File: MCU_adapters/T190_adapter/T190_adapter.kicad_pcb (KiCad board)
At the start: 2 copper layers, 35 x 60.6 mm, 5 parts, among them J1 Conn_01x22, J2 Conn_01x22, J3 Conn_01x12_Socket, J4 Conn_01x12_Socket

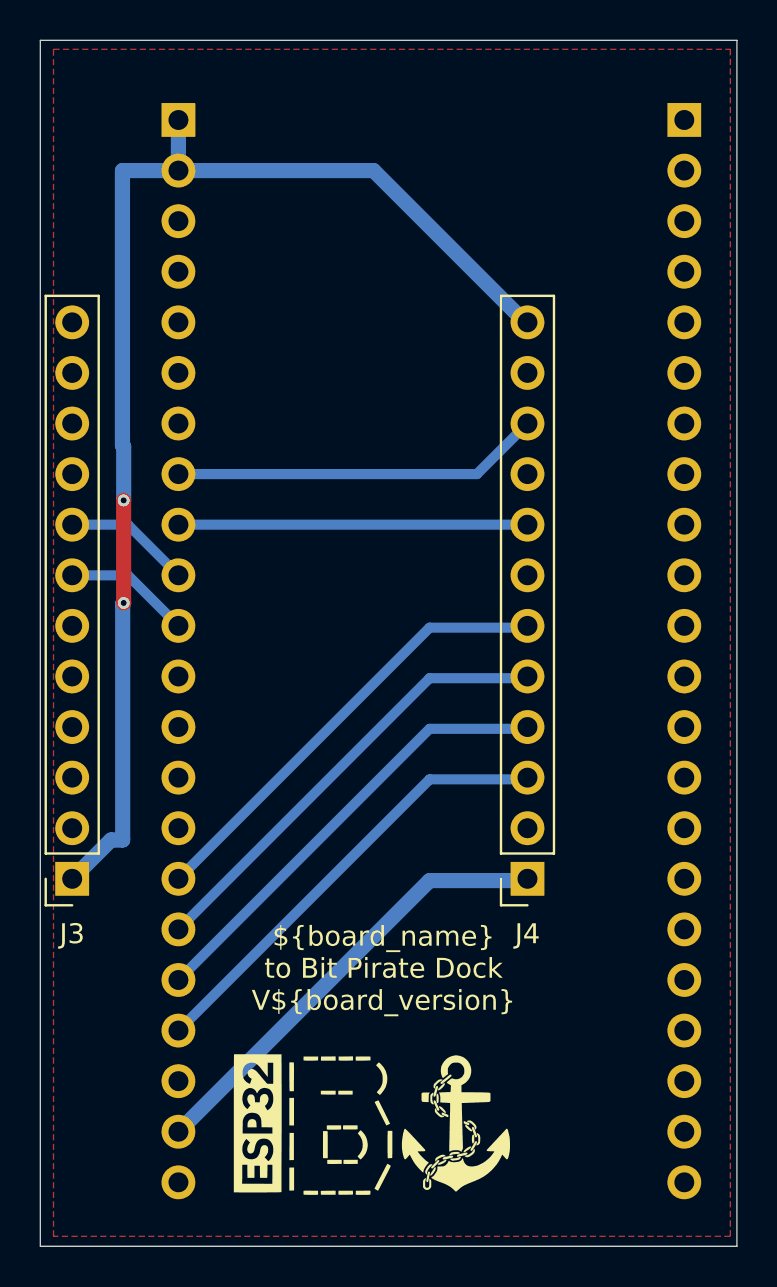
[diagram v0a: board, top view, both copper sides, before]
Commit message: Updated adapters with USB logo
Added an USB logo to ensure the card is inserted the right way up.
Added an USB logo in the logo library
Updated the gerber files
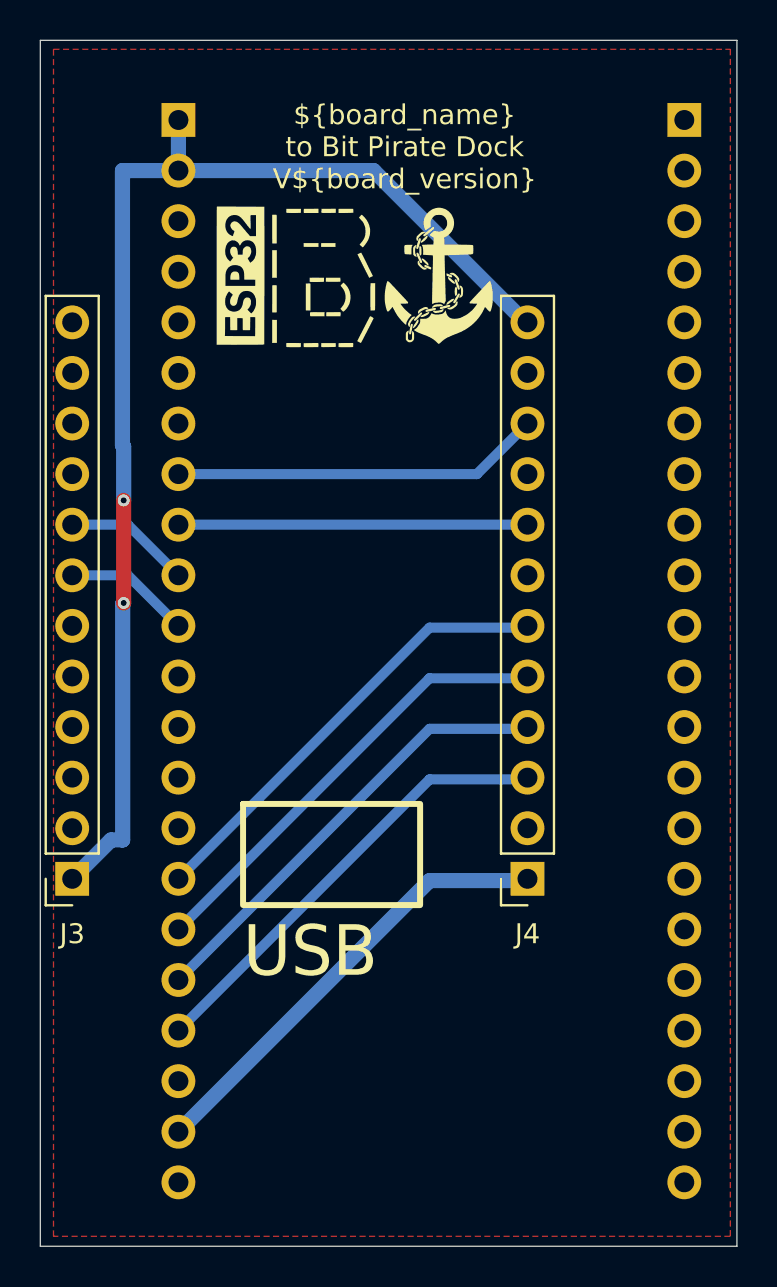
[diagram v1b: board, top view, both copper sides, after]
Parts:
- added G2: ~, logo:LOGO_USB, F.Cu at (84.5, 59.7)
- moved G1 42.6 mm to (84.9, 35.0)
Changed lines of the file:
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@@
 	(footprint "logo:logoBP"
 		(layer "F.Cu")
-		(at 85.773212 77.5912)
+		(at 84.91 35.03)
 		(property "Reference" "G1"
 			(at 0 -0.5 0)
@@
 		(embedded_fonts no)
 	)
+	(footprint "logo:LOGO_USB"
+		(layer "F.Cu")
+		(at 84.525 59.74)
+		(property "Reference" "G2"
+			(at 0 -0.5 0)
+			(unlocked yes)
+			(layer "F.SilkS")
+			(hide yes)
+			(effects
+				(font
+					(size 1 1)
+					(thickness 0.15)
+				)
+			)
+		)
+		(property "Value" "~"
+			(at 0 1 0)
+			(unlocked yes)
+			(layer "F.Fab")
+			(effects
+				(font
+					(size 1 1)
+					(thickness 0.15)
+				)
+			)
+		)
+		(property "Datasheet" ""
+			(at 0 0 0)
+			(unlocked yes)
+			(layer "F.Fab")
+			(hide yes)
+			(effects
+				(font
+					(size 1 1)
+					(thickness 0.15)
+				)
+			)
+		)
+		(property "Description" ""
+			(at 0 0 0)
+			(unlocked yes)
+			(layer "F.Fab")
+			(hide yes)
+			(effects
+				(font
+					(size 1 1)
+					(thickness 0.15)
+				)
+			)
+		)
+		(sheetname "/")
+		(sheetfile "T190_adapter.kicad_sch")
+		(units
+			(unit
+				(name "A")
+				(pins)
+			)
+		)
+		(attr smd exclude_from_bom)
+		(duplicate_pad_numbers_are_jumpers no)
+		(fp_rect
+			(start -5.08 0)
+			(end 3.81 5.08)
+			(stroke
+				(width 0.3)
+				(type solid)
+			)
+			(fill no)
+			(layer "F.SilkS")
+		)
+		(fp_text user "USB"
+			(at -5.08 8.89 0)
+			(unlocked yes)
+			(layer "F.SilkS")
+			(effects
+				(font
+					(size 2.54 2.4)
+					(thickness 0.25)
+				)
+				(justify left bottom)
+			)
+		)
+		(fp_text user "${REFERENCE}"
+			(at 0 2.5 0)
+			(unlocked yes)
+			(layer "F.Fab")
+			(effects
+				(font
+					(size 1 1)
+					(thickness 0.15)
+				)
+			)
+		)
+		(embedded_fonts no)
+	)
 	(footprint "Connector_PinHeader_2.54mm:PinHeader_1x22_P2.54mm_Vertical"
 		(locked yes)
@@
 	)
 	(gr_text "${board_name}\nto Bit Pirate Dock\nV${board_version}"
-		(at 86.5 70.2 0)
+		(at 87.56 28.95 0)
 		(layer "F.SilkS")
 		(effects
